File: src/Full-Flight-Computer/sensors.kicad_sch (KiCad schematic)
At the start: 37 parts, among them P4 440054-3, P5 440054-3, P6 440054-3, P7 440054-3, Q1 QS5U17TR, Q2 QS5U17TR, Q3 QS5U17TR, Q4 QS5U17TR, U12 BMM150, U3 BMI323, U4 MAX-8C-0-10, U5 BMP390

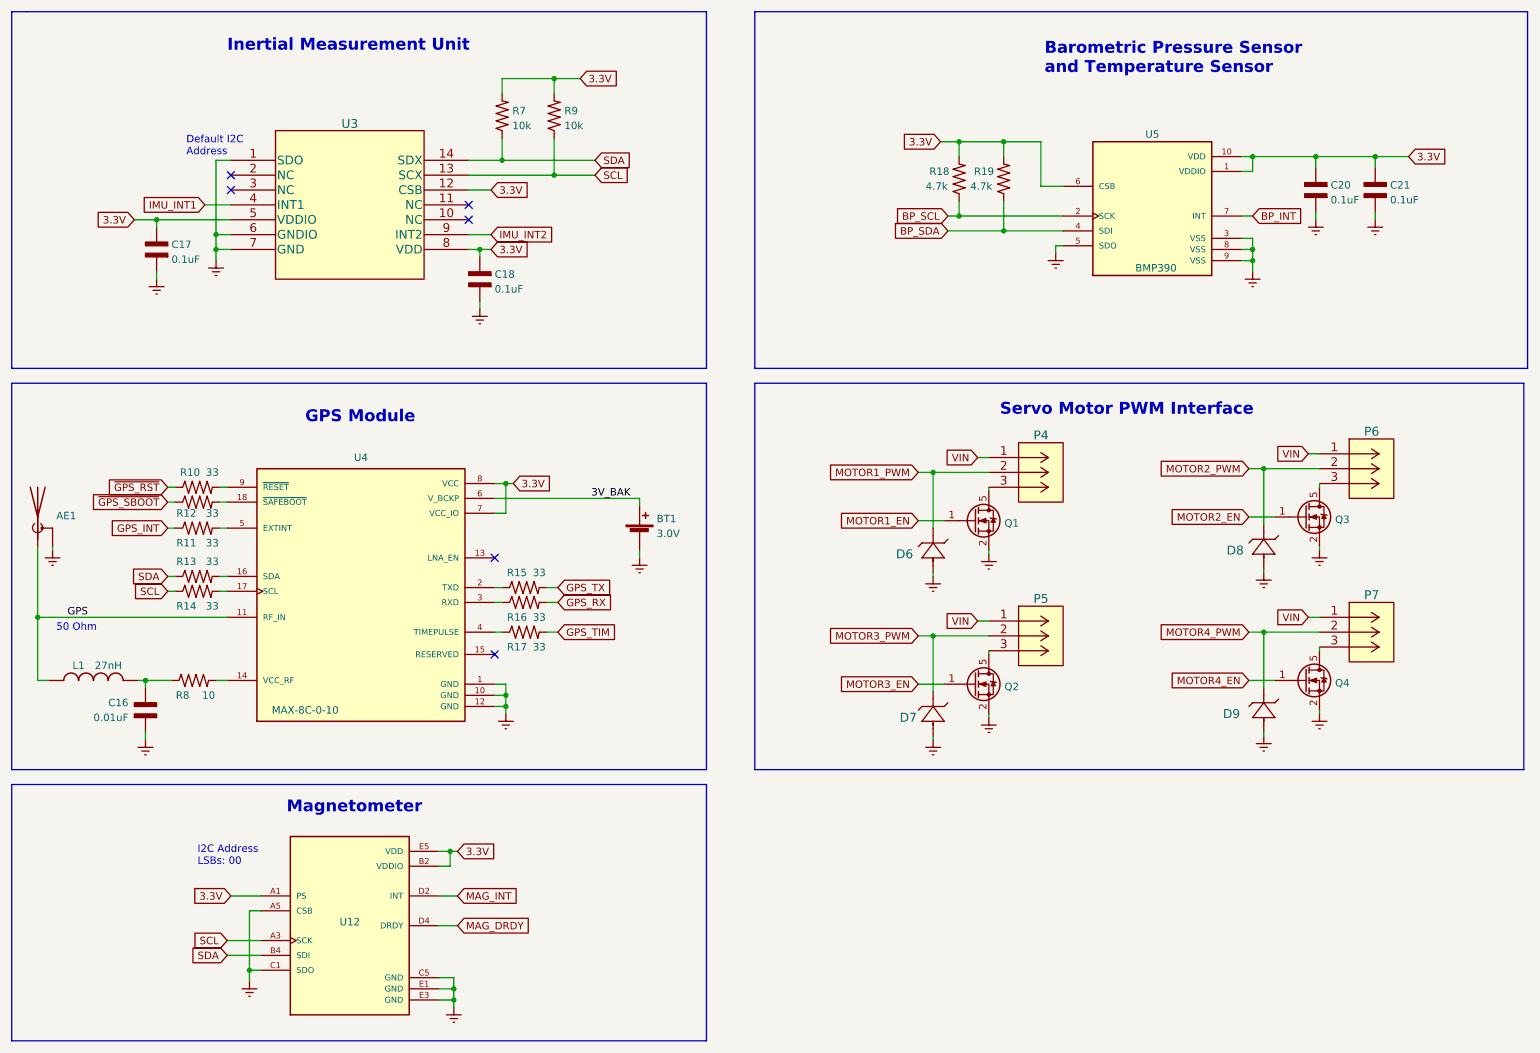
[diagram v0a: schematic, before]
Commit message: removed extra sections from schematic
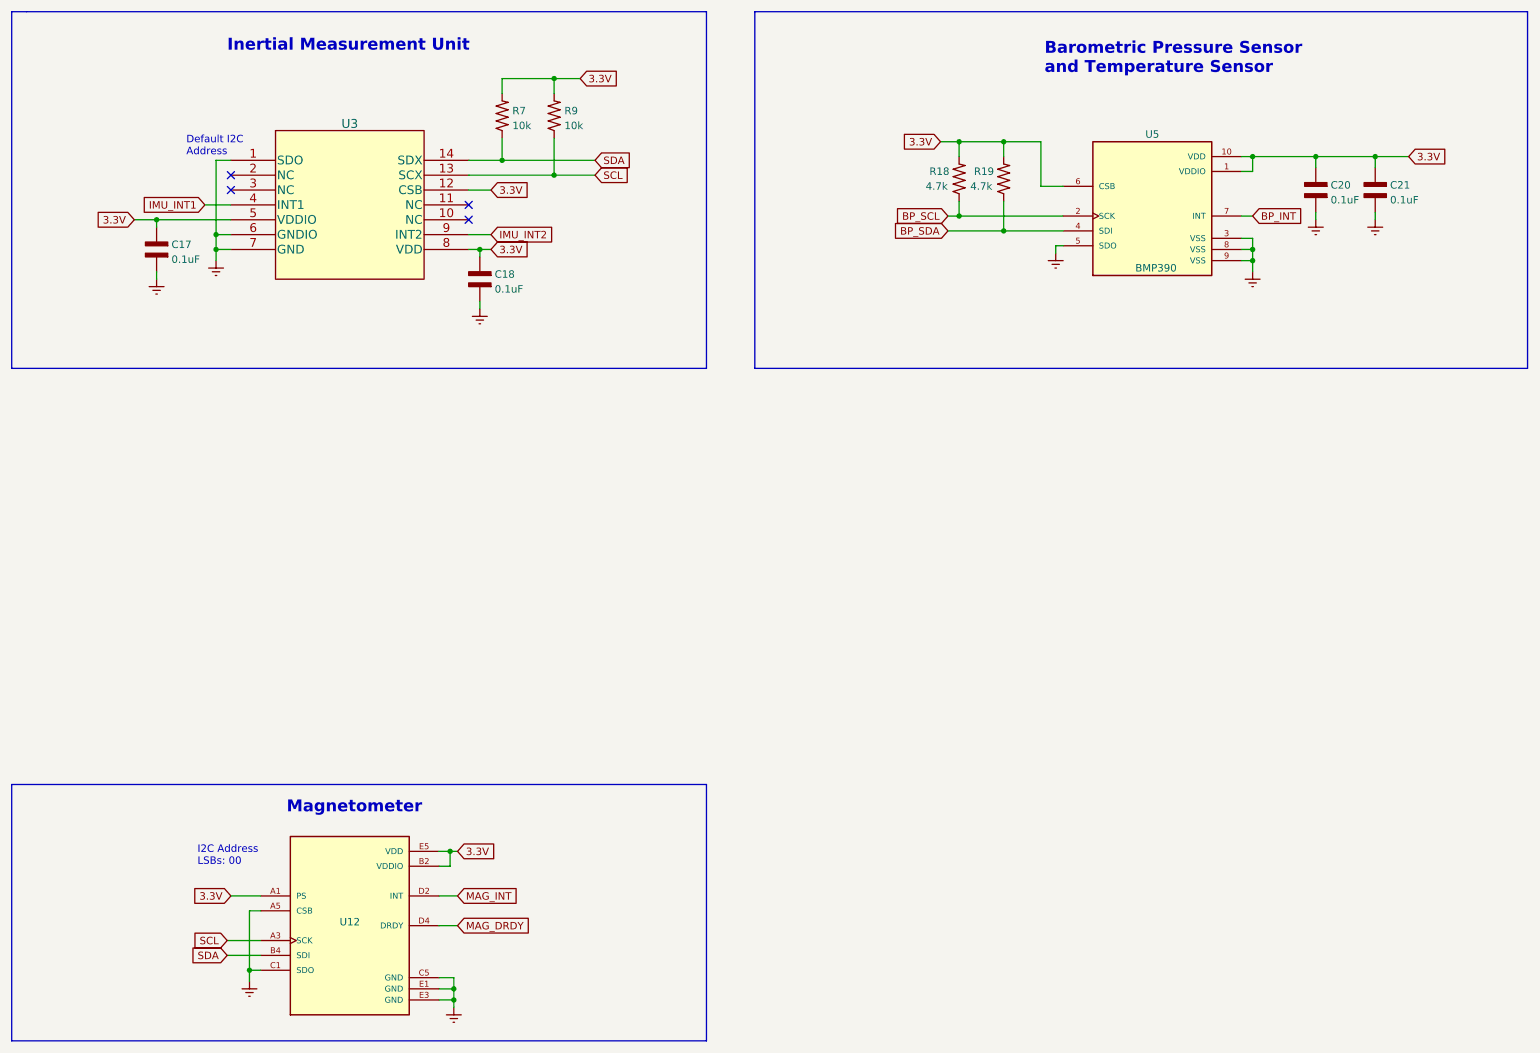
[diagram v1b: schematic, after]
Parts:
- removed AE1: 0734120110, Flight-Computer:73412-0110, symbol Flight-Computer:0734120110
- removed BT1: MS614SE-FL28E, Flight-Computer:MS621FE-FL11E, symbol Flight-Computer:MS614SE-FL28E
- removed C16: 0.01uF, Flight-Computer:CAP_0603, symbol Flight-Computer:CAP_0603
- removed D6, D7, D8, D9: MM3Z3V3B, Flight-Computer:MM3Z3V3B, symbol Flight-Computer:MM3Z3V3B
- removed L1: 27nH, Flight-Computer:L-07C27NJV6T, symbol Flight-Computer:L-07C27NJV6T
- removed P4, P5, P6, P7: 440054-3, Flight-Computer:440054-3, symbol Flight-Computer:440054-3
- removed Q1, Q2, Q3, Q4: QS5U17TR, Flight-Computer:QS5U17TR, symbol Flight-Computer:QS5U17TR
- removed R10, R11, R12, R13, R14, R15, R16, R17: 33, Flight-Computer:RES_0603, symbol Flight-Computer:RES_0603
- removed R8: 10, Flight-Computer:RES_0603, symbol Flight-Computer:RES_0603
- removed U4: MAX-8C-0-10, Flight-Computer:MAX-8C-0, symbol Flight-Computer:MAX-8C-0-10
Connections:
- no-connect marks 6 -> 4
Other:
- note removed: "50 Ohm"
- note removed: "GPS Module"
- note removed: "Servo Motor PWM Interface"

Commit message: fixed all schematic symbol links to link to correct lib file
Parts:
- C17, C18, C20, C21: footprint Flight-Computer:CAP_0603 -> Full-Flight-Computer:CAP_0402; symbol Flight-Computer:CAP_0603 -> Full-Flight-Computer:CAP_0402
- R18, R19: footprint Flight-Computer:RES_0603 -> Full-Flight-Computer:RES_0402; symbol Flight-Computer:RES_0603 -> Full-Flight-Computer:RES_0402
- R7, R9: footprint Engine-Controller:RES_0603 -> Full-Flight-Computer:RES_0402; symbol Flight-Computer:RES_0603 -> Full-Flight-Computer:RES_0402
- U12: footprint Flight-Computer:BMM150 -> Full-Flight-Computer:BMM150; symbol Flight-Computer:BMM150 -> Full-Flight-Computer:BMM150
- U3: footprint Flight-Computer:BMI323 -> Full-Flight-Computer:BMI323; symbol Flight-Computer:BMI323 -> Full-Flight-Computer:BMI323
- U5: footprint Flight-Computer:BMP390 -> Full-Flight-Computer:BMP390; symbol Flight-Computer:BMP390 -> Full-Flight-Computer:BMP390
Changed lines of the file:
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@@
     )
   )
-  (symbol (lib_id "Flight-Computer:Earth") (at 59.055 183.515 0) (unit 1)
+  (symbol (lib_id "Full-Flight-Computer:Earth") (at 59.055 183.515 0) (unit 1)
     (in_bom yes) (on_board yes) (dnp no) (fields_autoplaced)
     (property "Reference" "#PWR020" (at 59.055 189.865 0)
@@
     )
   )
-  (symbol (lib_id "Flight-Computer:RES_0603") (at 111.125 35.56 90) (unit 1)
+  (symbol (lib_id "Full-Flight-Computer:RES_0402") (at 111.125 35.56 90) (unit 1)
     (in_bom yes) (on_board yes) (dnp no) (fields_autoplaced)
     (property "Reference" "R9" (at 112.8776 34.7253 90)
@@
       (effects (font (size 1.27 1.27)) (justify right))
     )
-    (property "Footprint" "Engine-Controller:RES_0603" (at 123.825 34.29 0)
+    (property "Footprint" "Full-Flight-Computer:RES_0402" (at 123.825 34.29 0)
       (effects (font (size 1.27 1.27)) (justify left bottom) hide)
     )
@@
     )
   )
-  (symbol (lib_id "Flight-Computer:Earth") (at 53.34 60.325 0) (unit 1)
+  (symbol (lib_id "Full-Flight-Computer:Earth") (at 53.34 60.325 0) (unit 1)
     (in_bom yes) (on_board yes) (dnp no) (fields_autoplaced)
     (property "Reference" "#PWR016" (at 53.34 66.675 0)
@@
     )
   )
-  (symbol (lib_id "Flight-Computer:RES_0603") (at 180.34 46.355 90) (unit 1)
+  (symbol (lib_id "Full-Flight-Computer:RES_0402") (at 180.34 46.355 90) (unit 1)
     (in_bom yes) (on_board yes) (dnp no)
     (property "Reference" "R18" (at 175.26 45.085 90)
@@
       (effects (font (size 1.27 1.27)) (justify right))
     )
-    (property "Footprint" "Flight-Computer:RES_0603" (at 193.04 45.085 0)
+    (property "Footprint" "Full-Flight-Computer:RES_0402" (at 193.04 45.085 0)
       (effects (font (size 1.27 1.27)) (justify left bottom) hide)
     )
@@
     )
   )
-  (symbol (lib_id "Flight-Computer:CAP_0603") (at 241.3 48.26 90) (unit 1)
+  (symbol (lib_id "Full-Flight-Computer:CAP_0402") (at 241.3 48.26 90) (unit 1)
     (in_bom yes) (on_board yes) (dnp no) (fields_autoplaced)
     (property "Reference" "C20" (at 243.84 47.4253 90)
@@
       (effects (font (size 1.27 1.27)) (justify right))
     )
-    (property "Footprint" "Flight-Computer:CAP_0603" (at 251.46 50.8 0)
+    (property "Footprint" "Full-Flight-Computer:CAP_0402" (at 251.46 50.8 0)
       (effects (font (size 1.27 1.27)) (justify left bottom) hide)
     )
@@
     )
   )
-  (symbol (lib_id "Flight-Computer:Earth") (at 230.505 62.23 0) (unit 1)
+  (symbol (lib_id "Full-Flight-Computer:Earth") (at 230.505 62.23 0) (unit 1)
     (in_bom yes) (on_board yes) (dnp no) (fields_autoplaced)
     (property "Reference" "#PWR028" (at 230.505 68.58 0)
@@
     )
   )
-  (symbol (lib_id "Flight-Computer:RES_0603") (at 187.96 46.355 90) (unit 1)
+  (symbol (lib_id "Full-Flight-Computer:RES_0402") (at 187.96 46.355 90) (unit 1)
     (in_bom yes) (on_board yes) (dnp no)
     (property "Reference" "R19" (at 182.88 45.085 90)
@@
       (effects (font (size 1.27 1.27)) (justify right))
     )
-    (property "Footprint" "Flight-Computer:RES_0603" (at 200.66 45.085 0)
+    (property "Footprint" "Full-Flight-Computer:RES_0402" (at 200.66 45.085 0)
       (effects (font (size 1.27 1.27)) (justify left bottom) hide)
     )
@@
     )
   )
-  (symbol (lib_id "Flight-Computer:BMP390") (at 213.36 52.705 0) (unit 1)
+  (symbol (lib_id "Full-Flight-Computer:BMP390") (at 213.36 52.705 0) (unit 1)
     (in_bom yes) (on_board yes) (dnp no)
     (property "Reference" "U5" (at 213.36 38.735 0)
@@
       (effects (font (size 1.27 1.27)))
     )
-    (property "Footprint" "Flight-Computer:BMP390" (at 205.74 67.31 0)
+    (property "Footprint" "Full-Flight-Computer:BMP390" (at 205.74 67.31 0)
       (effects (font (size 1.27 1.27)) (justify left bottom) hide)
     )
@@
     )
   )
-  (symbol (lib_id "Flight-Computer:Earth") (at 98.425 68.58 0) (unit 1)
+  (symbol (lib_id "Full-Flight-Computer:Earth") (at 98.425 68.58 0) (unit 1)
     (in_bom yes) (on_board yes) (dnp no) (fields_autoplaced)
     (property "Reference" "#PWR018" (at 98.425 74.93 0)
@@
     )
   )
-  (symbol (lib_id "Flight-Computer:CAP_0603") (at 98.425 63.5 90) (unit 1)
+  (symbol (lib_id "Full-Flight-Computer:CAP_0402") (at 98.425 63.5 90) (unit 1)
     (in_bom yes) (on_board yes) (dnp no) (fields_autoplaced)
     (property "Reference" "C18" (at 100.965 62.6653 90)
@@
       (effects (font (size 1.27 1.27)) (justify right))
     )
-    (property "Footprint" "Flight-Computer:CAP_0603" (at 108.585 66.04 0)
+    (property "Footprint" "Full-Flight-Computer:CAP_0402" (at 108.585 66.04 0)
       (effects (font (size 1.27 1.27)) (justify left bottom) hide)
     )
@@
     )
   )
-  (symbol (lib_id "Flight-Computer:Earth") (at 93.98 187.96 0) (unit 1)
+  (symbol (lib_id "Full-Flight-Computer:Earth") (at 93.98 187.96 0) (unit 1)
     (in_bom yes) (on_board yes) (dnp no) (fields_autoplaced)
     (property "Reference" "#PWR021" (at 93.98 194.31 0)
@@
     )
   )
-  (symbol (lib_id "Flight-Computer:Earth") (at 241.3 53.34 0) (unit 1)
+  (symbol (lib_id "Full-Flight-Computer:Earth") (at 241.3 53.34 0) (unit 1)
     (in_bom yes) (on_board yes) (dnp no) (fields_autoplaced)
     (property "Reference" "#PWR033" (at 241.3 59.69 0)
@@
     )
   )
-  (symbol (lib_id "Flight-Computer:Earth") (at 196.85 59.055 0) (unit 1)
+  (symbol (lib_id "Full-Flight-Computer:Earth") (at 196.85 59.055 0) (unit 1)
     (in_bom yes) (on_board yes) (dnp no) (fields_autoplaced)
     (property "Reference" "#PWR027" (at 196.85 65.405 0)
@@
     )
   )
-  (symbol (lib_id "Flight-Computer:Earth") (at 251.46 53.34 0) (unit 1)
+  (symbol (lib_id "Full-Flight-Computer:Earth") (at 251.46 53.34 0) (unit 1)
     (in_bom yes) (on_board yes) (dnp no) (fields_autoplaced)
     (property "Reference" "#PWR034" (at 251.46 59.69 0)
@@
     )
   )
-  (symbol (lib_id "Flight-Computer:Earth") (at 43.18 63.5 0) (unit 1)
+  (symbol (lib_id "Full-Flight-Computer:Earth") (at 43.18 63.5 0) (unit 1)
     (in_bom yes) (on_board yes) (dnp no) (fields_autoplaced)
     (property "Reference" "#PWR017" (at 43.18 69.85 0)
@@
     )
   )
-  (symbol (lib_id "Flight-Computer:RES_0603") (at 102.235 35.56 90) (unit 1)
+  (symbol (lib_id "Full-Flight-Computer:RES_0402") (at 102.235 35.56 90) (unit 1)
     (in_bom yes) (on_board yes) (dnp no) (fields_autoplaced)
     (property "Reference" "R7" (at 103.9876 34.7253 90)
@@
       (effects (font (size 1.27 1.27)) (justify right))
     )
-    (property "Footprint" "Engine-Controller:RES_0603" (at 114.935 34.29 0)
+    (property "Footprint" "Full-Flight-Computer:RES_0402" (at 114.935 34.29 0)
       (effects (font (size 1.27 1.27)) (justify left bottom) hide)
     )
@@
     )
   )
-  (symbol (lib_id "Flight-Computer:CAP_0603") (at 43.18 58.42 90) (unit 1)
+  (symbol (lib_id "Full-Flight-Computer:CAP_0402") (at 43.18 58.42 90) (unit 1)
     (in_bom yes) (on_board yes) (dnp no) (fields_autoplaced)
     (property "Reference" "C17" (at 45.72 57.5853 90)
@@
       (effects (font (size 1.27 1.27)) (justify right))
     )
-    (property "Footprint" "Flight-Computer:CAP_0603" (at 53.34 60.96 0)
+    (property "Footprint" "Full-Flight-Computer:CAP_0402" (at 53.34 60.96 0)
       (effects (font (size 1.27 1.27)) (justify left bottom) hide)
     )
@@
     )
   )
-  (symbol (lib_id "Flight-Computer:BMI323") (at 55.88 43.18 0) (unit 1)
+  (symbol (lib_id "Full-Flight-Computer:BMI323") (at 55.88 43.18 0) (unit 1)
     (in_bom yes) (on_board yes) (dnp no) (fields_autoplaced)
     (property "Reference" "U3" (at 76.2 36.9331 0)
@@
       (effects (font (size 1.524 1.524)) hide)
     )
-    (property "Footprint" "Flight-Computer:BMI323" (at 76.2 37.084 0)
+    (property "Footprint" "Full-Flight-Computer:BMI323" (at 76.2 37.084 0)
       (effects (font (size 1.524 1.524)) hide)
     )
@@
     )
   )
-  (symbol (lib_id "Flight-Computer:CAP_0603") (at 251.46 48.26 90) (unit 1)
+  (symbol (lib_id "Full-Flight-Computer:CAP_0402") (at 251.46 48.26 90) (unit 1)
     (in_bom yes) (on_board yes) (dnp no) (fields_autoplaced)
     (property "Reference" "C21" (at 254 47.4253 90)
@@
       (effects (font (size 1.27 1.27)) (justify right))
     )
-    (property "Footprint" "Flight-Computer:CAP_0603" (at 261.62 50.8 0)
+    (property "Footprint" "Full-Flight-Computer:CAP_0402" (at 261.62 50.8 0)
       (effects (font (size 1.27 1.27)) (justify left bottom) hide)
     )
@@
     )
   )
-  (symbol (lib_id "Flight-Computer:BMM150") (at 76.2 173.99 0) (unit 1)
+  (symbol (lib_id "Full-Flight-Computer:BMM150") (at 76.2 173.99 0) (unit 1)
     (in_bom yes) (on_board yes) (dnp no)
     (property "Reference" "U12" (at 76.2 173.355 0)
@@
       (effects (font (size 1.27 1.27)) (justify left top) hide)
     )
-    (property "Footprint" "Flight-Computer:BMM150" (at 93.98 202.565 0)
+    (property "Footprint" "Full-Flight-Computer:BMM150" (at 93.98 202.565 0)
       (effects (font (size 1.27 1.27)) (justify bottom) hide)
     )
